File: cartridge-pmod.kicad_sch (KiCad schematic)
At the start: 25 parts, among them J1 2.54-2*6P Bend insert, J2 CONFIG, J3 PJ-320B, U1 W25Q128JVSIM, U2 878-APS6404L-3SQR-SN, U4 74LVCE1G126SE-7

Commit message: ERC clean: add PWR_FLAG on filtered VCCA rail; export schematic PDF
KiCad 10.0.4 ERC now passes with 0 errors (the 71 remaining warnings are
missing-global-library noise from a CLI-only install, all symbols embedded).

Co-Authored-By: Claude Fable 5 <noreply@anthropic.com>
Claude-Session: https://claude.ai/code/session_01Xe5NzHvb72amxJFhr7WjZC
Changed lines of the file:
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@@
 		)
+	)
+	(symbol
+		(lib_id "power:PWR_FLAG")
+		(at 203.2 146.05 270)
+		(unit 1)
+		(exclude_from_sim no)
+		(in_bom yes)
+		(on_board yes)
+		(dnp no)
+		(fields_autoplaced yes)
+		(property "Reference" "#FLG03"
+			(at 205.1 146.05 0)
+			(effects
+				(font
+					(size 1.27 1.27)
+				)
+				(hide yes)
+			)
+		)
+		(property "Value" "PWR_FLAG"
+			(at 207.01 146.05 90)
+			(effects
+				(font
+					(size 1.27 1.27)
+				)
+				(justify left)
+				(hide yes)
+			)
+		)
+		(property "Footprint" ""
+			(at 203.2 146.05 0)
+			(effects
+				(font
+					(size 1.27 1.27)
+				)
+				(hide yes)
+			)
+		)
+		(property "Datasheet" "~"
+			(at 203.2 146.05 0)
+			(effects
+				(font
+					(size 1.27 1.27)
+				)
+				(hide yes)
+			)
+		)
+		(property "Description" ""
+			(at 203.2 146.05 0)
+			(effects
+				(font
+					(size 1.27 1.27)
+				)
+				(hide yes)
+			)
+		)
+		(pin "1"
+		)
+		(instances
+			(project "tiny-vga"
+				(path "/48d88fc2-ef96-4320-9e25-3db84dc2dfb5"
+					(reference "#FLG03")
+					(unit 1)
+				)
+			)
+			(project "qspi-pmod"
+				(path "/702ec277-2284-48d6-94f3-5b91c08910c1"
+					(reference "#FLG03")
+					(unit 1)
+				)
+			)
+		)
+	)
+	(wire
+		(pts
+			(xy 203.2 146.05) (xy 203.2 149.86)
+		)
+		(stroke
+			(width 0)
+			(type default)
+		)
+	)
+	(junction
+		(at 203.2 149.86)
+		(diameter 0)
+		(color 0 0 0 0)
 	)
 	(sheet_instances

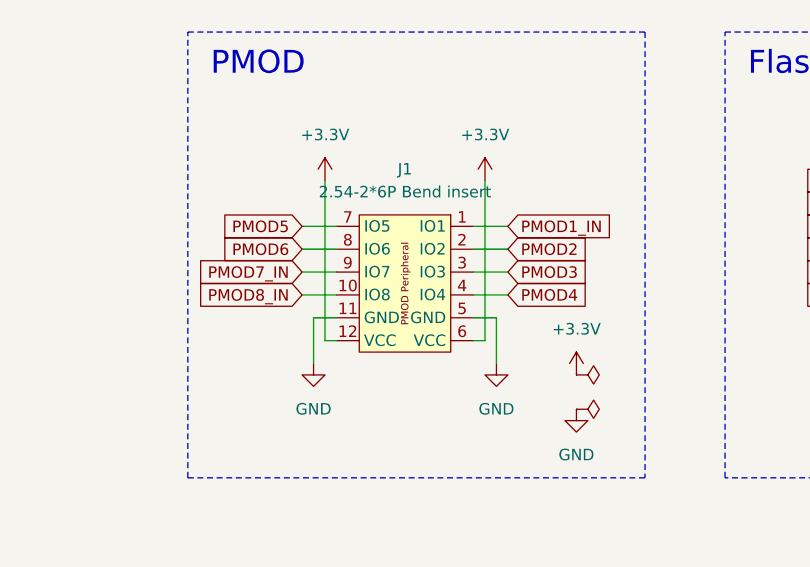
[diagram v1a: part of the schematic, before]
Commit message: Push LCSC supplier fields to board; first Fabrication Toolkit export
F8 field sync so the toolkit reads LCSC Part from footprints (audio-section
numbers exported blank before). production/ holds the JLC BOM/CPL/gerber zip.

Co-Authored-By: Claude Fable 5 <noreply@anthropic.com>
Claude-Session: https://claude.ai/code/session_01KoqFR2y5XeXxq4PQckdZZA
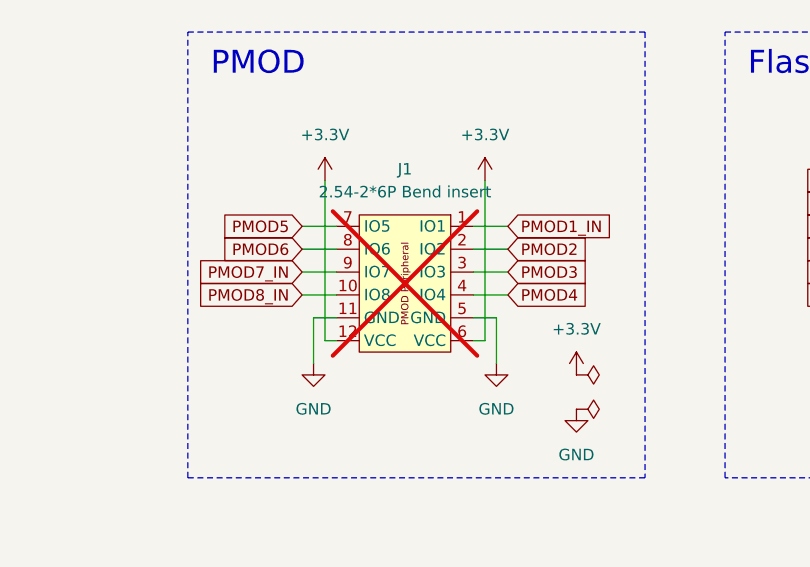
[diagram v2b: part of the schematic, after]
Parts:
- J1: now not fitted
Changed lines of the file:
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@@
 		(in_bom yes)
 		(on_board yes)
-		(dnp no)
+		(dnp yes)
 		(property "Reference" "J1"
 			(at 71.12 81.28 0)

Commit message: Silk cleanup + J1 promoted to JLC-assembled
- Delete J1's 24 off-board silk pin drawings (18 silk_edge_clearance
  warnings -> 0; fab would clip them, connector body covers the area)
- Nudge C11/C12/R5 label row off C13's pads; un-hide C13 and R6 labels
- Clear DNP on J1 (board + schematic): C60565 header now in JLC BOM/CPL
  for economic THT assembly; J2 stays DNP (solder-jumper pattern)
- Regenerate production/ via headless Fabrication Toolkit (-t -f -e -nI)
- FABRICATION.md: document new J1 status + headless export recipe

DRC after: 0 unconnected, 0 silk, only the 23 known-ignorable baseline
errors (22 CONFIG cut-trace + 1 upstream starved thermal). ERC 0.

Co-Authored-By: Claude Fable 5 <noreply@anthropic.com>
Claude-Session: https://claude.ai/code/session_01KoqFR2y5XeXxq4PQckdZZA
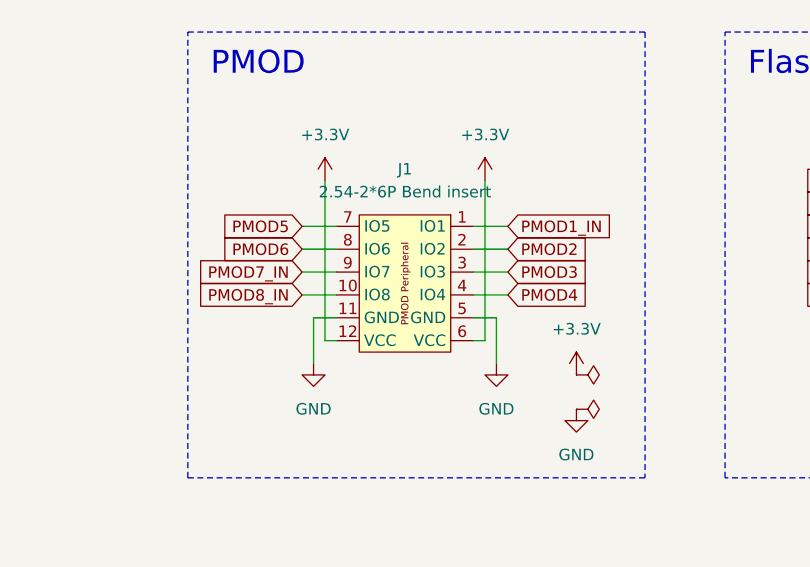
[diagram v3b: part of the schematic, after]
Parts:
- J1: now fitted
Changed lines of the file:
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@@
 		(in_bom yes)
 		(on_board yes)
-		(dnp yes)
+		(dnp no)
 		(property "Reference" "J1"
 			(at 71.12 81.28 0)
